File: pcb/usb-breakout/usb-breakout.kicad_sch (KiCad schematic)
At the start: 7 parts, among them CN1 S7B-ZR-SM4A-TF(LF)(SN)_C51187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

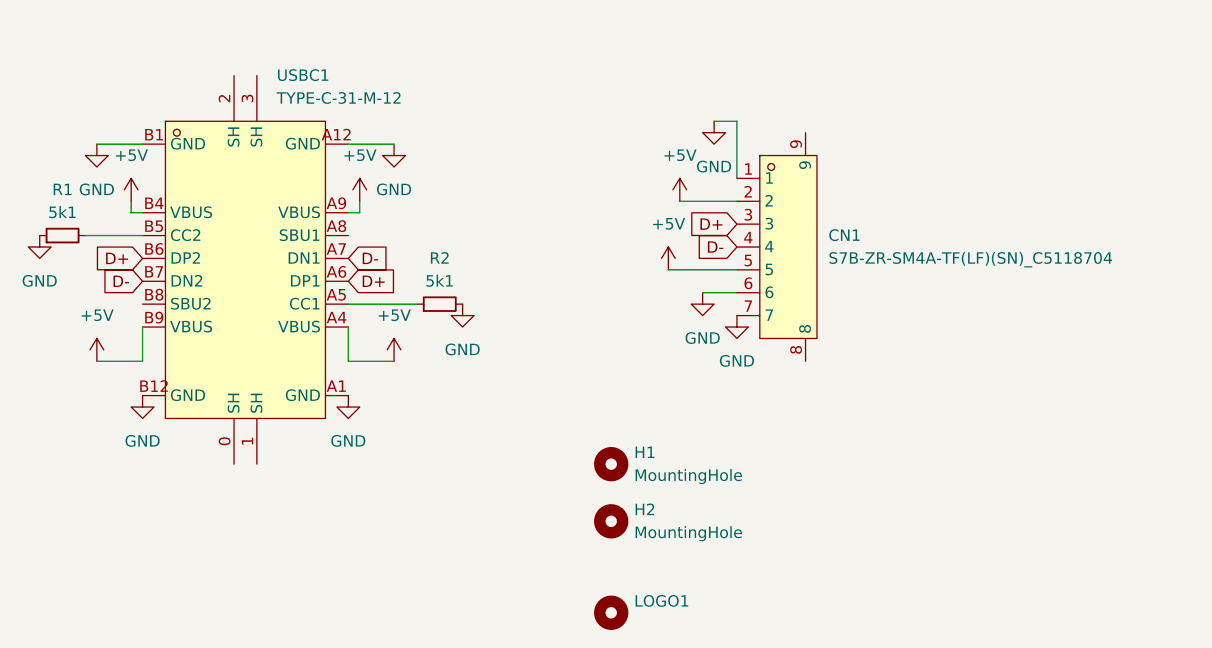
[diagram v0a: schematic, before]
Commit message: NG | Update usb ext pinout, cleanup
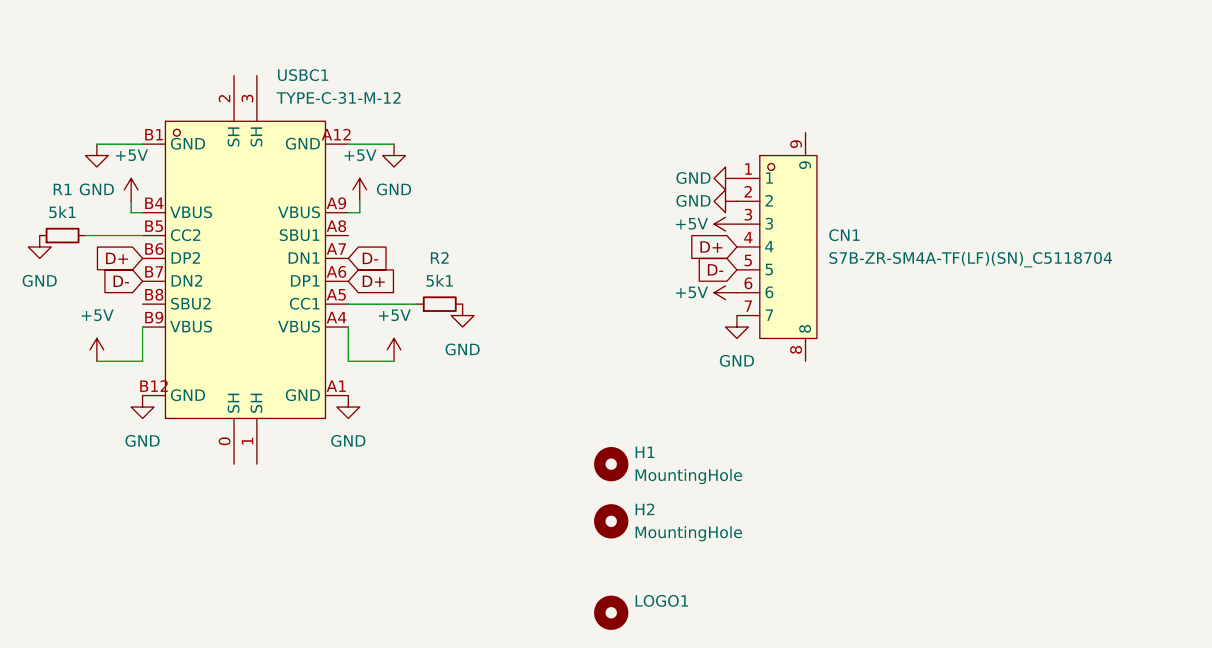
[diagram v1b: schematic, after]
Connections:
- net +5V: now also CN1.3, CN1.6; no longer CN1.2, CN1.5
- net D+: now also CN1.4; no longer CN1.3
- net D-: now also CN1.5; no longer CN1.4
- net GND: now also CN1.2; no longer CN1.6
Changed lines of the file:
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@@
 	(wire
 		(pts
-			(xy 127 44.45) (xy 133.35 44.45)
+			(xy 67.31 62.23) (xy 67.31 58.42)
 		)
 		(stroke
@@
 	(wire
 		(pts
-			(xy 67.31 62.23) (xy 67.31 58.42)
+			(xy 62.23 38.1) (xy 67.31 38.1)
 		)
 		(stroke
@@
 	(wire
 		(pts
-			(xy 62.23 38.1) (xy 67.31 38.1)
+			(xy 90.17 55.88) (xy 97.79 55.88)
 		)
 		(stroke
@@
 	(wire
 		(pts
-			(xy 130.81 35.56) (xy 133.35 35.56)
+			(xy 66.04 45.72) (xy 67.31 45.72)
 		)
 		(stroke
@@
 	(wire
 		(pts
-			(xy 90.17 55.88) (xy 97.79 55.88)
+			(xy 90.17 58.42) (xy 90.17 62.23)
 		)
 		(stroke
@@
 	(wire
 		(pts
-			(xy 66.04 45.72) (xy 67.31 45.72)
+			(xy 91.44 45.72) (xy 91.44 44.45)
 		)
 		(stroke
@@
 	(wire
 		(pts
-			(xy 90.17 58.42) (xy 90.17 62.23)
+			(xy 90.17 38.1) (xy 95.25 38.1)
 		)
 		(stroke
@@
 	(wire
 		(pts
-			(xy 91.44 45.72) (xy 91.44 44.45)
+			(xy 90.17 45.72) (xy 91.44 45.72)
 		)
 		(stroke
@@
 	(wire
 		(pts
-			(xy 125.73 52.07) (xy 133.35 52.07)
+			(xy 90.17 62.23) (xy 95.25 62.23)
 		)
 		(stroke
@@
 		)
 	)
-	(wire
-		(pts
-			(xy 133.35 35.56) (xy 133.35 41.91)
-		)
-		(stroke
-			(width 0)
-			(type default)
-		)
-	)
-	(wire
-		(pts
-			(xy 90.17 38.1) (xy 95.25 38.1)
-		)
-		(stroke
-			(width 0)
-			(type default)
-		)
-	)
-	(wire
-		(pts
-			(xy 90.17 45.72) (xy 91.44 45.72)
-		)
-		(stroke
-			(width 0)
-			(type default)
-		)
-	)
-	(wire
-		(pts
-			(xy 90.17 62.23) (xy 95.25 62.23)
-		)
-		(stroke
-			(width 0)
-			(type default)
-		)
-	)
-	(wire
-		(pts
-			(xy 129.54 54.61) (xy 133.35 54.61)
-		)
-		(stroke
-			(width 0)
-			(type default)
-		)
-	)
 	(global_label "D+"
 		(shape input)
@@
 	(global_label "D-"
 		(shape input)
-		(at 133.35 49.53 180)
+		(at 133.35 52.07 180)
 		(fields_autoplaced yes)
 		(effects
@@
 		)
 		(property "Intersheetrefs" "${INTERSHEET_REFS}"
-			(at 127.5224 49.53 0)
+			(at 127.5224 52.07 0)
 			(effects
 				(font
@@
 	(global_label "D+"
 		(shape input)
-		(at 133.35 46.99 180)
+		(at 133.35 49.53 180)
 		(fields_autoplaced yes)
 		(effects
@@
 		)
 		(property "Intersheetrefs" "${INTERSHEET_REFS}"
-			(at 127.5224 46.99 0)
+			(at 127.5224 49.53 0)
 			(effects
 				(font
@@
 	(symbol
 		(lib_id "power:GND")
-		(at 130.81 35.56 0)
-		(unit 1)
-		(exclude_from_sim no)
-		(in_bom yes)
-		(on_board yes)
-		(dnp no)
-		(fields_autoplaced yes)
+		(at 133.35 41.91 270)
+		(unit 1)
+		(exclude_from_sim no)
+		(in_bom yes)
+		(on_board yes)
+		(dnp no)
 		(property "Reference" "#PWR013"
-			(at 130.81 41.91 0)
+			(at 127 41.91 0)
 			(effects
 				(font
@@
 		)
 		(property "Value" "GND"
-			(at 130.81 40.64 0)
+			(at 128.524 41.91 90)
 			(effects
 				(font
@@
 		)
 		(property "Footprint" ""
-			(at 130.81 35.56 0)
+			(at 133.35 41.91 0)
 			(effects
 				(font
@@
 		)
 		(property "Datasheet" ""
-			(at 130.81 35.56 0)
+			(at 133.35 41.91 0)
 			(effects
 				(font
@@
 		)
 		(property "Description" "Power symbol creates a global label with name \"GND\" , ground"
-			(at 130.81 35.56 0)
+			(at 133.35 41.91 0)
 			(effects
 				(font
@@
 	(symbol
 		(lib_id "power:+5V")
-		(at 127 44.45 0)
-		(unit 1)
-		(exclude_from_sim no)
-		(in_bom yes)
-		(on_board yes)
-		(dnp no)
-		(fields_autoplaced yes)
+		(at 133.35 54.61 90)
+		(unit 1)
+		(exclude_from_sim no)
+		(in_bom yes)
+		(on_board yes)
+		(dnp no)
 		(property "Reference" "#PWR012"
-			(at 127 48.26 0)
+			(at 137.16 54.61 0)
 			(effects
 				(font
@@
 		)
 		(property "Value" "+5V"
-			(at 127 39.37 0)
+			(at 128.27 54.61 90)
 			(effects
 				(font
@@
 		)
 		(property "Footprint" ""
-			(at 127 44.45 0)
+			(at 133.35 54.61 0)
 			(effects
 				(font
@@
 		)
 		(property "Datasheet" ""
-			(at 127 44.45 0)
+			(at 133.35 54.61 0)
 			(effects
 				(font
@@
 		)
 		(property "Description" "Power symbol creates a global label with name \"+5V\""
-			(at 127 44.45 0)
+			(at 133.35 54.61 0)
 			(effects
 				(font
@@
 	(symbol
 		(lib_id "power:+5V")
-		(at 125.73 52.07 0)
-		(unit 1)
-		(exclude_from_sim no)
-		(in_bom yes)
-		(on_board yes)
-		(dnp no)
-		(fields_autoplaced yes)
+		(at 133.35 46.99 90)
+		(unit 1)
+		(exclude_from_sim no)
+		(in_bom yes)
+		(on_board yes)
+		(dnp no)
 		(property "Reference" "#PWR014"
-			(at 125.73 55.88 0)
+			(at 137.16 46.99 0)
 			(effects
 				(font
@@
 		)
 		(property "Value" "+5V"
-			(at 125.73 46.99 0)
+			(at 128.27 46.99 90)
 			(effects
 				(font
@@
 		)
 		(property "Footprint" ""
-			(at 125.73 52.07 0)
+			(at 133.35 46.99 0)
 			(effects
 				(font
@@
 		)
 		(property "Datasheet" ""
-			(at 125.73 52.07 0)
+			(at 133.35 46.99 0)
 			(effects
 				(font
@@
 		)
 		(property "Description" "Power symbol creates a global label with name \"+5V\""
-			(at 125.73 52.07 0)
+			(at 133.35 46.99 0)
 			(effects
 				(font
@@
 	(symbol
 		(lib_id "power:GND")
-		(at 129.54 54.61 0)
-		(unit 1)
-		(exclude_from_sim no)
-		(in_bom yes)
-		(on_board yes)
-		(dnp no)
-		(fields_autoplaced yes)
+		(at 133.35 44.45 270)
+		(unit 1)
+		(exclude_from_sim no)
+		(in_bom yes)
+		(on_board yes)
+		(dnp no)
 		(property "Reference" "#PWR015"
-			(at 129.54 60.96 0)
+			(at 127 44.45 0)
 			(effects
 				(font
@@
 		)
 		(property "Value" "GND"
-			(at 129.54 59.69 0)
+			(at 128.524 44.45 90)
 			(effects
 				(font
@@
 		)
 		(property "Footprint" ""
-			(at 129.54 54.61 0)
+			(at 133.35 44.45 0)
 			(effects
 				(font
@@
 		)
 		(property "Datasheet" ""
-			(at 129.54 54.61 0)
+			(at 133.35 44.45 0)
 			(effects
 				(font
@@
 		)
 		(property "Description" "Power symbol creates a global label with name \"GND\" , ground"
-			(at 129.54 54.61 0)
-			(effects
-				(font
+			(at 133.35 44.45 0)
+			(effects
+				(font

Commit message: NG | Splitfox PCB Placement
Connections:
- net GND: now also CN1.8, CN1.9, USBC1.0 (SH), USBC1.1 (SH), USBC1.2 (SH), USBC1.3 (SH)
